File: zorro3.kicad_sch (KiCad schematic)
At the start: 17 parts, among them CN1 Zorro3, U1 CY74FCT16543TPVCT, U11 SN74ABT16374ADGGR, U12 74LVC07APW_118, U13 SN74ABT16245ADGGR, U14 74ACT521MTCX, U2 CY74FCT16543TPVCT, U3 CY74FCT16543TPVCT, U5 CY74FCT543ATQCT

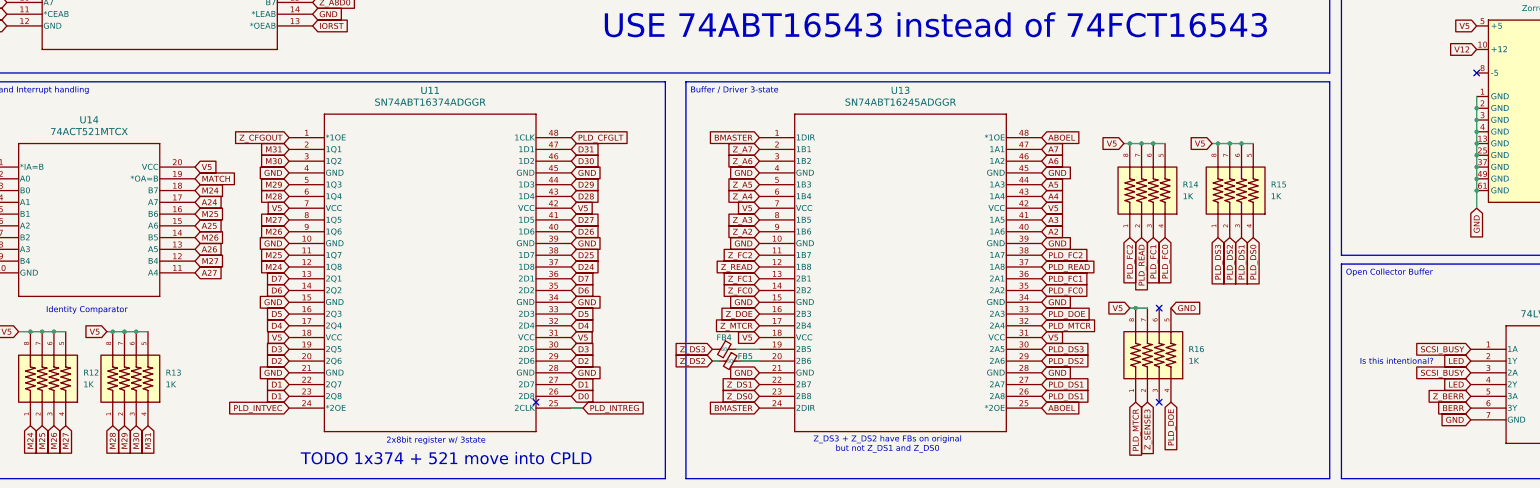
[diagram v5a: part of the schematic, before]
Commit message: Update RN footprint to CAY16_102J4LF
- Rename RNs from R to RN.
- Fix U5 footprint
- Rename pages to be consecutive numbers
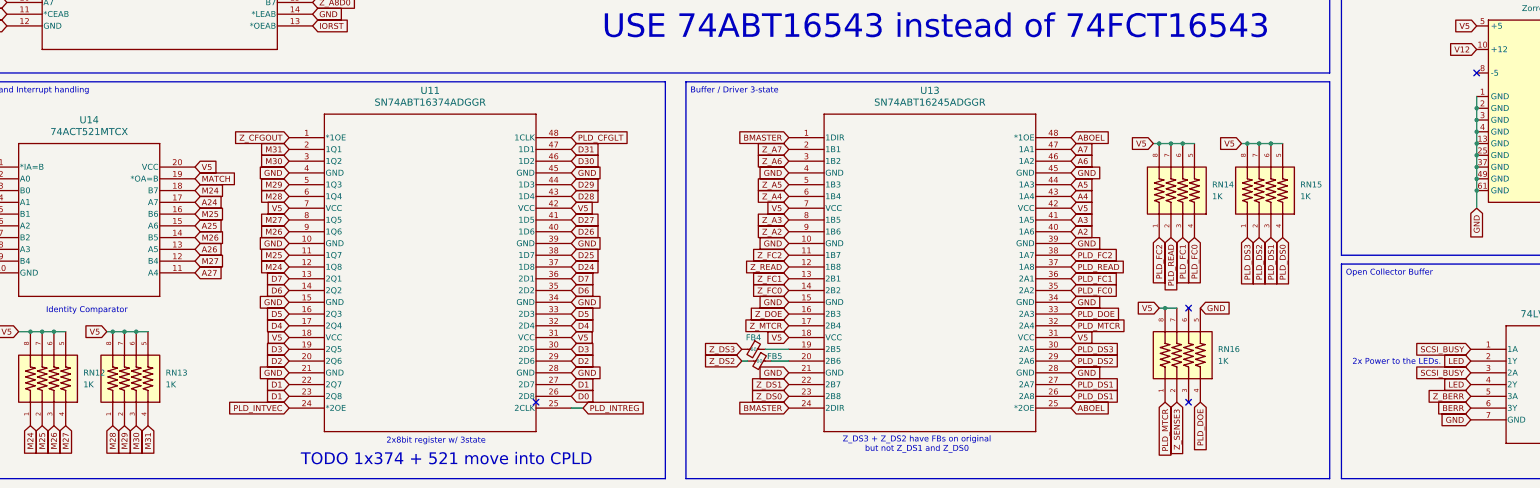
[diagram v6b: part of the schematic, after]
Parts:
- RN12: renamed from R12; footprint YC324-FK-071KL:RESCAXS127P508X320X70-8N -> CAY16_102J4LF:BO_CAY16
- RN13: renamed from R13; footprint YC324-FK-071KL:RESCAXS127P508X320X70-8N -> CAY16_102J4LF:BO_CAY16
- RN14: renamed from R14; footprint YC324-FK-071KL:RESCAXS127P508X320X70-8N -> CAY16_102J4LF:BO_CAY16
- RN15: renamed from R15; footprint YC324-FK-071KL:RESCAXS127P508X320X70-8N -> CAY16_102J4LF:BO_CAY16
- RN16: renamed from R16; footprint YC324-FK-071KL:RESCAXS127P508X320X70-8N -> CAY16_102J4LF:BO_CAY16
- U5: footprint 74FCT16543:DL56 -> CY74FCT543ATQCT:DBQ24
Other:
- note added: "2x Power to the LEDs."
- note removed: "Is this intentional?"
- moved on the sheet: FB4, FB5, RN14, RN15, RN16, U13

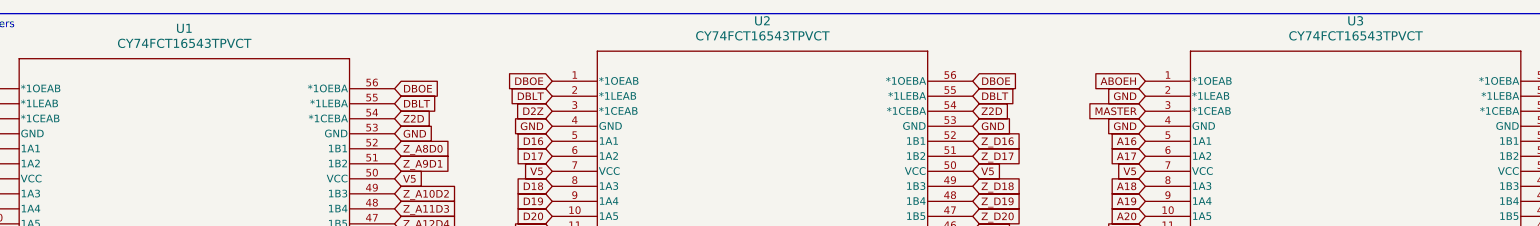
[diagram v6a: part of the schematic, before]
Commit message: Switch to 74ABT16543
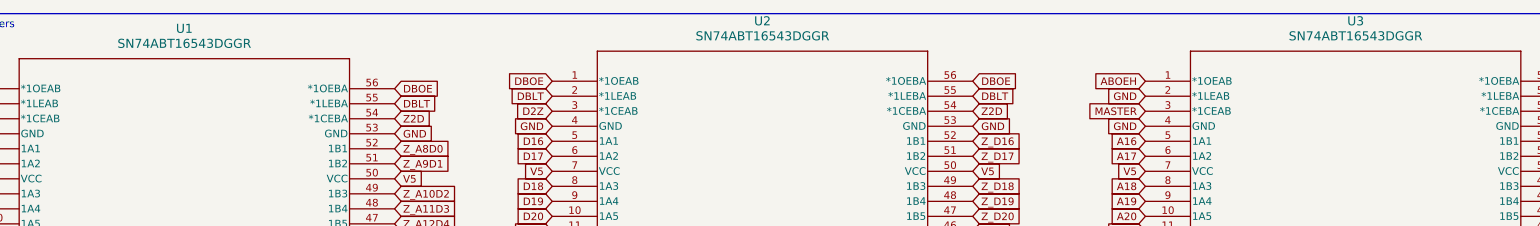
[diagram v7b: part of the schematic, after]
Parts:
- U1, U2, U3: value CY74FCT16543TPVCT -> SN74ABT16543DGGR
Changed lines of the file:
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@@
 			)
 		)
-		(property "Value" "CY74FCT16543TPVCT"
+		(property "Value" "SN74ABT16543DGGR"
 			(at 261.62 19.05 0)
 			(effects
@@
 			)
 		)
-		(property "Datasheet" "CY74FCT16543TPVCT"
+		(property "Datasheet" "https://www.ti.com/lit/ds/symlink/sn74abt16543.pdf"
 			(at 226.06 26.67 0)
 			(effects
@@
 			)
 		)
-		(property "Value" "CY74FCT16543TPVCT"
+		(property "Value" "SN74ABT16543DGGR"
 			(at 63.5 20.32 0)
 			(effects
@@
 			)
 		)
-		(property "Datasheet" "CY74FCT16543TPVCT"
+		(property "Datasheet" "https://www.ti.com/lit/ds/symlink/sn74abt16543.pdf"
 			(at 27.94 27.94 0)
 			(effects
@@
 			)
 		)
-		(property "Value" "CY74FCT16543TPVCT"
+		(property "Value" "SN74ABT16543DGGR"
 			(at 161.29 19.05 0)
 			(effects
@@
 			)
 		)
-		(property "Datasheet" "CY74FCT16543TPVCT"
+		(property "Datasheet" "https://www.ti.com/lit/ds/symlink/sn74abt16543.pdf"
 			(at 125.73 26.67 0)
 			(effects

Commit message: Remove ABT TODO
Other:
- note removed: "USE 74ABT16543 instead of 74FCT16543"
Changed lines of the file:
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@@
 	(generator_version "9.0")
 	(paper "A3")
-	(text "USE 74ABT16543 instead of 74FCT16543"
-		(exclude_from_sim no)
-		(at 228.6 151.384 0)
-		(effects
-			(font
-				(size 5.08 5.08)
-			)
-		)
-	)
 	(text "Z_DS3 + Z_DS2 have FBs on original\nbut not Z_DS1 and Z_DS0"
 		(exclude_from_sim no)
